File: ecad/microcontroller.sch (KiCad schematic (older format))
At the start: 2 parts, among them J4 Nucleo_F446_LHS, J5 Nucleo_F446_RHS

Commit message: Change Pin PA5 to PC7. Create two way communication scheme. UNTESTED
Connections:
- net PC7 is gone; now on net DB14: J5.19 (Pin_19)
- net DB14: no longer J5.11 (Pin_11)
- new net PA5: J5.11 (Pin_11)
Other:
- note added: "Orig PA5 was used here, \nbut it caused strange \nproblems so PA 11 is \nused instead."
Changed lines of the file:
@@
 May be issues with all of PC13, \nPC14 and PC15 due to battery \nmanagement system.
 NoConn ~ 6700 2650
-Text Label 6950 3000 0    60   ~ 0
-PA5
 Text Notes 6500 2250 0    60   ~ 0
 Cut and relocate these traces
@@
 Wire Notes Line
 	7800 2300 6550 2300
+Text Notes 6650 3550 0    60   ~ 0
+Orig PA5 was used here, \nbut it caused strange \nproblems so PA 11 is \nused instead.
+Text Label 6950 3000 0    60   ~ 0
+PC7
 $EndSCHEMATC

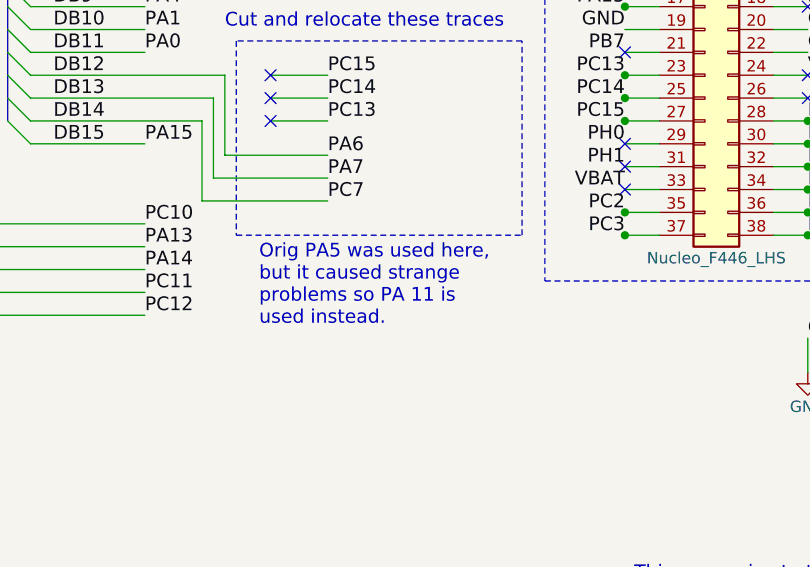
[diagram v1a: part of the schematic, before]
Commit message: Hardware changes for bias voltage osc fix and planned preamp gain correction part selection.
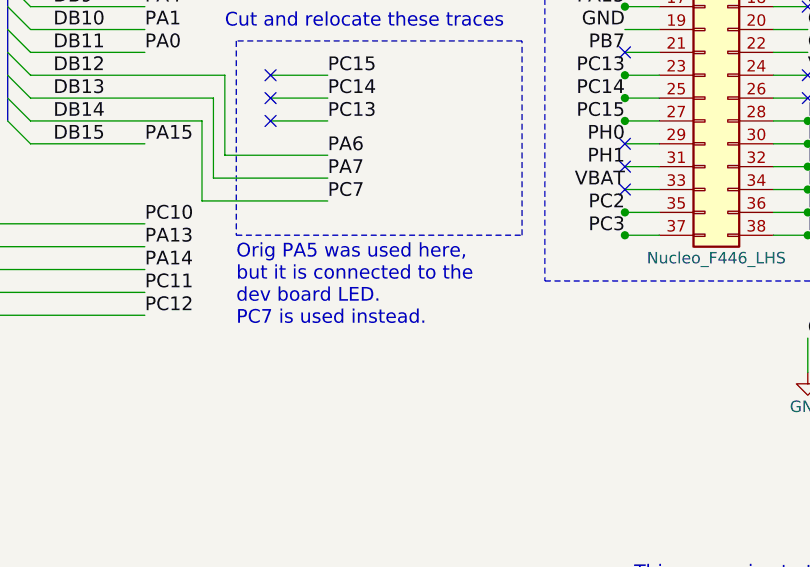
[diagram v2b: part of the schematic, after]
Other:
- note added: "Orig PA5 was used here, \nbut it is connected to the \ndev board LED. \nPC7 is used instead."
- note removed: "Orig PA5 was used here, \nbut it caused strange \nproblems so PA 11 is \nused instead."
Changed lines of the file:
@@
 Wire Notes Line
 	7800 2300 6550 2300
-Text Notes 6650 3550 0    60   ~ 0
-Orig PA5 was used here, \nbut it caused strange \nproblems so PA 11 is \nused instead.
+Text Notes 6550 3550 0    60   ~ 0
+Orig PA5 was used here, \nbut it is connected to the \ndev board LED. \nPC7 is used instead.
 Text Label 6950 3000 0    60   ~ 0
 PC7

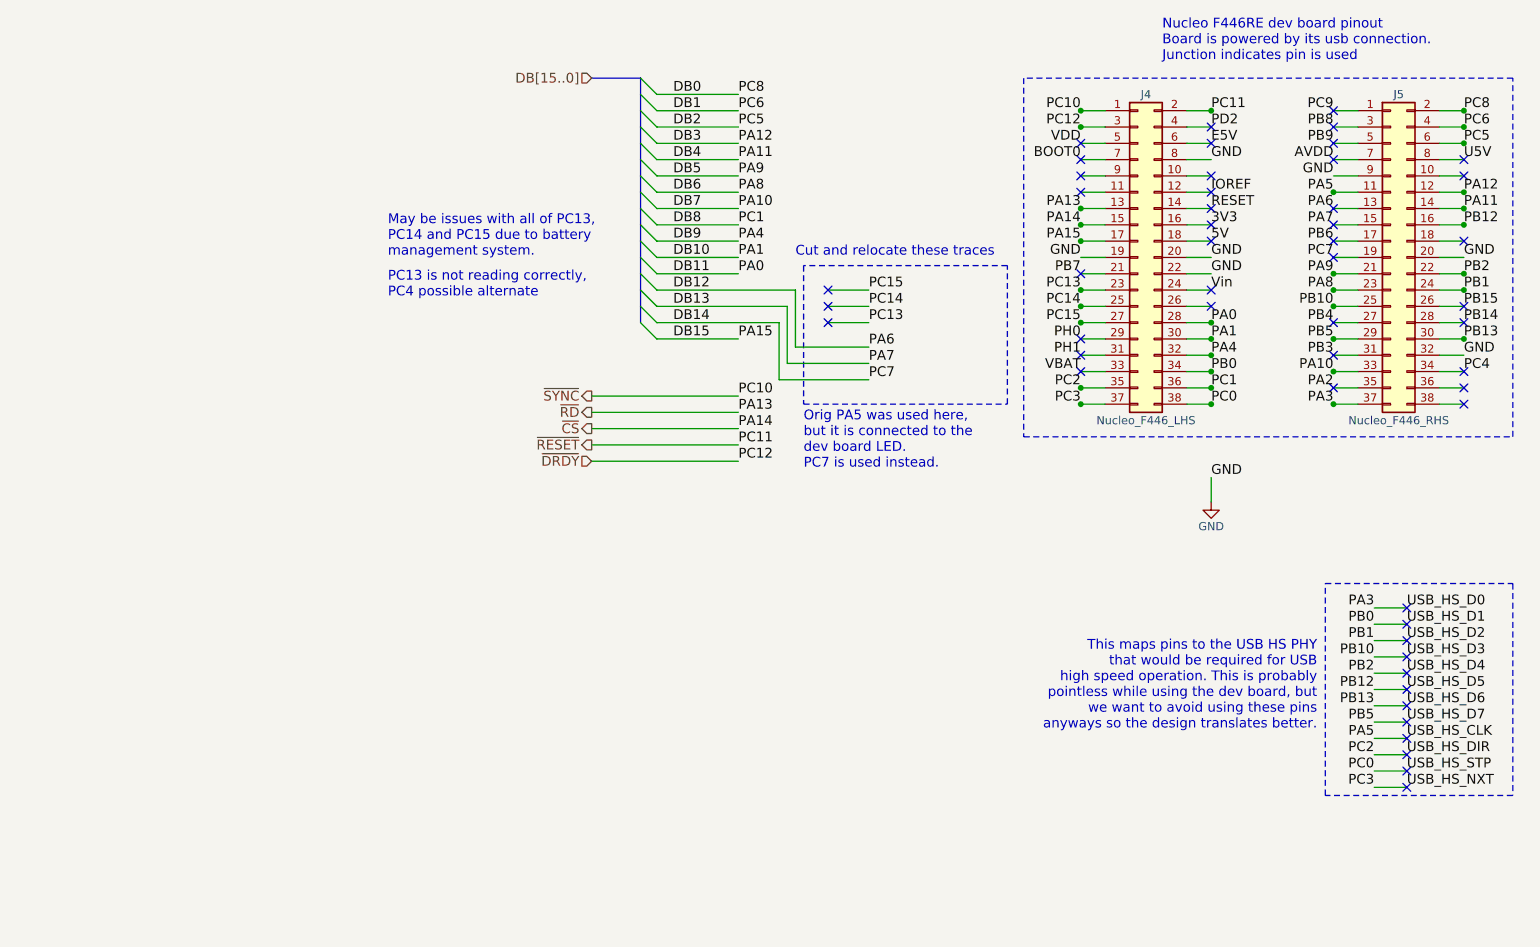
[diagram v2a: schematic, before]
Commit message: Slight changes to simulation and ecad with new changes before rollback to old changes.
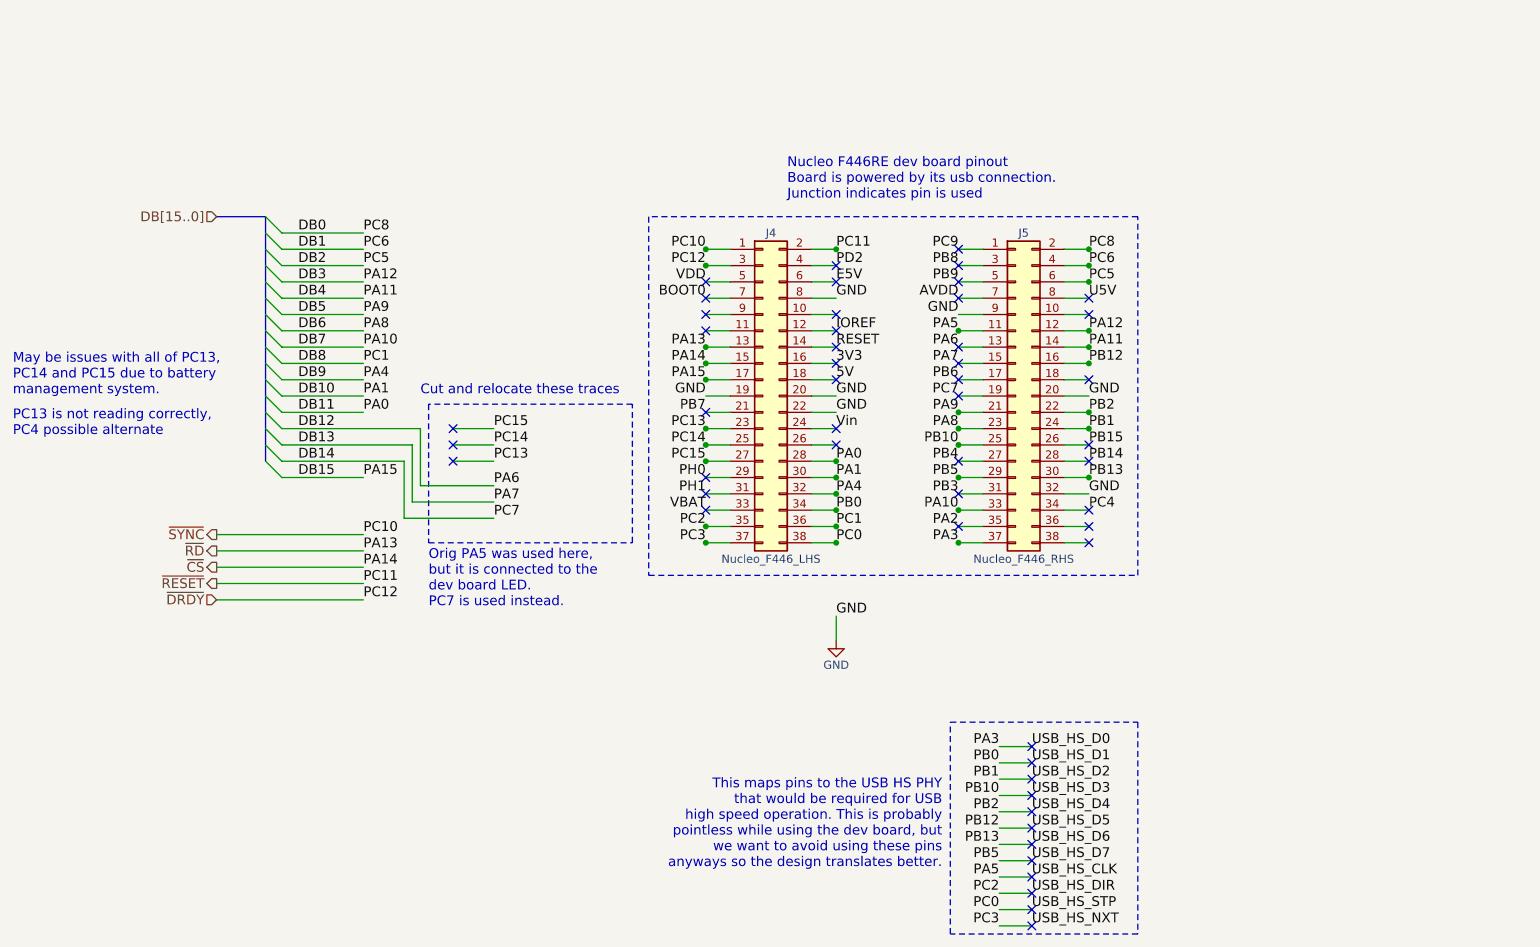
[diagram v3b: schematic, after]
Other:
- moved on the sheet: J4, J5

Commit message: Commit it all and let God^H^H^H diff sort it out.
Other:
- note added: "PC15:PC13 \nare part of \nbattery \nmanagement \nand don't \nlike to be \nGPIO"
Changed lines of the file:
@@
 Text Label 4650 3850 0    60   ~ 0
 PC7
+Text Notes 4900 3900 0    60   ~ 0
+PC15:PC13 \nare part of \nbattery \nmanagement \nand don't \nlike to be \nGPIO
 $EndSCHEMATC
